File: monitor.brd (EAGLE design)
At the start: 149.3 x 84.8 mm, 60 parts, among them IC1 LM1117-5, IC2 LM1117-5, J3 DCJ0202, J4 DCJ0202, J5 DCJ0202, Q1 IRLML2502, T1 BC846, X3 PN61729-S, X4 PN87520-S

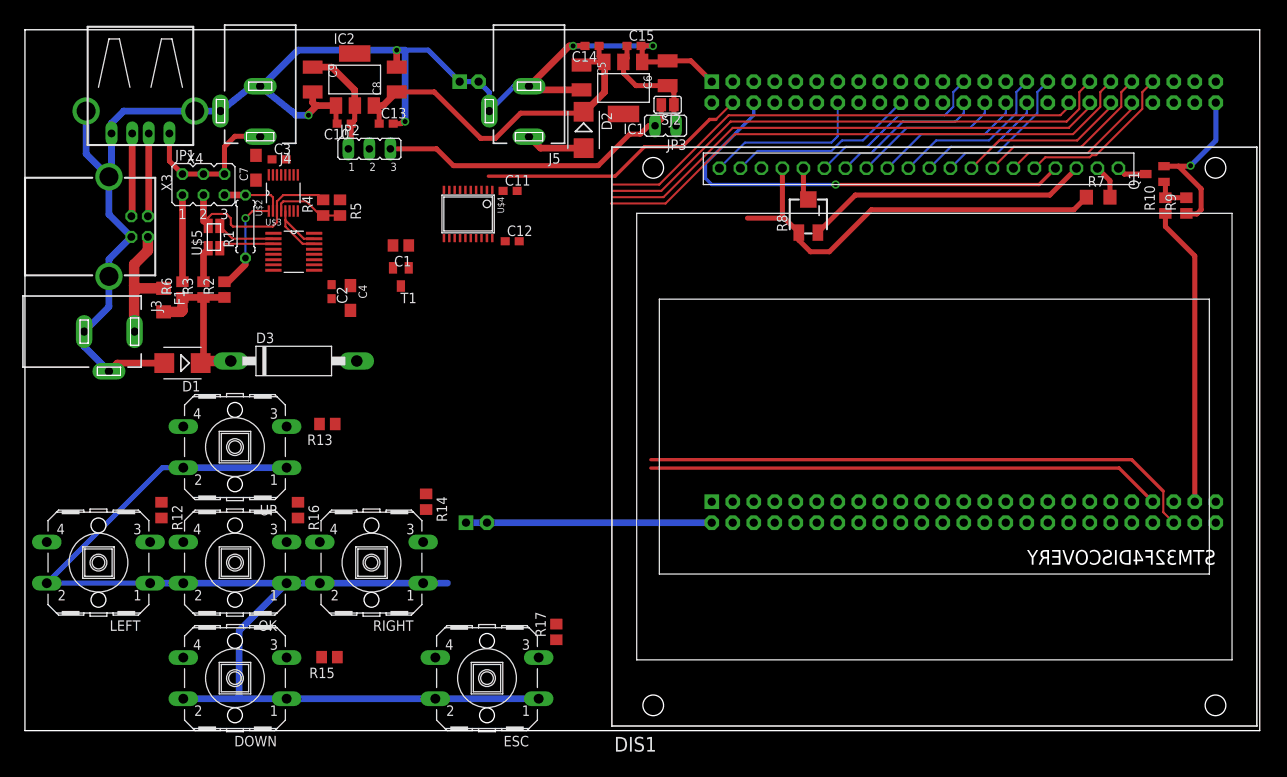
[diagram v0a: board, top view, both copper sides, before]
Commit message: SPI to PGA
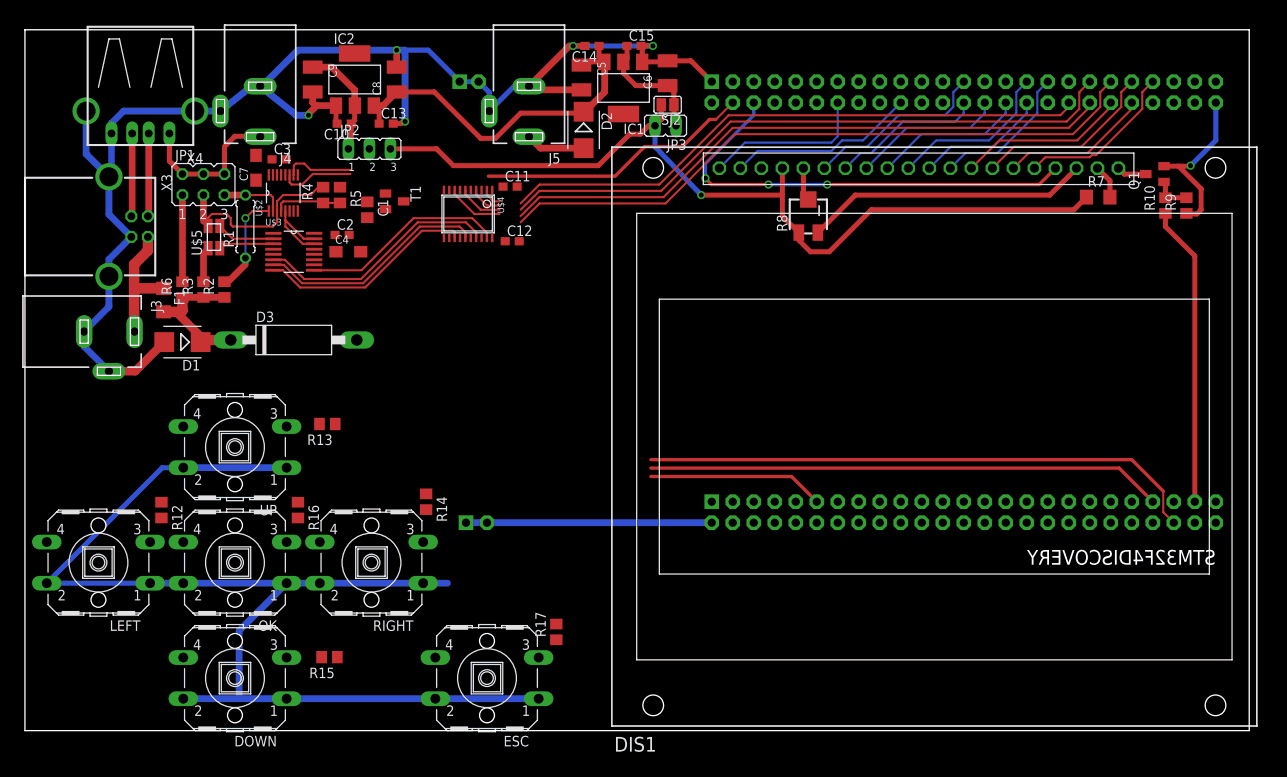
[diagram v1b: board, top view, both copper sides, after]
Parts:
- moved T1 9.18 mm to (44.7, 64.0), turned to 270 degrees
- moved C2 6.97 mm to (38.4, 59.9), turned to 0 degrees
- moved C1 5.93 mm to (41.4, 63.0), turned to 270 degrees
- moved C4 5.59 mm to (39.1, 57.9), turned to 0 degrees
- moved D1 2.54 mm to (19.1, 47.0)
- moved D3 2.54 mm to (32.5, 47.2)
- moved R4 1.52 mm to (36.1, 64.8)
- moved R5 1.52 mm to (38.1, 64.8)
- moved C11 0.51 mm to (58.7, 65.8)
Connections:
- new net OE: U$1.P$61, U$4.11
- net /CS: now also U$4.17; no longer U$4.19
- net CLK: now also U$4.13; no longer U$4.3
- net DIN: now also U$4.15; no longer U$4.5
- net DOUT: now also U$4.19; no longer U$4.17
- net I2C3_SCL: now also U$4.12; no longer U$4.14
- net I2C3_SDA: now also U$4.14; no longer U$4.6
- net SCL: now also U$4.9; no longer U$4.7
- net SDA: now also U$4.7; no longer U$4.15
- net SPI2_MISO: now also U$4.2; no longer U$4.4
- net SPI2_MOSI: now also U$4.6; no longer U$4.16
- net SPI2_NSS: now also U$4.4; no longer U$4.2
- net SPI2_SCK: now also U$4.8; no longer U$4.18
- net VDD: no longer U$1.P$72
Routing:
- net /CS: track 0.00 -> 29.5 mm
- net DIN: track 0.00 -> 28.0 mm
- net CLK: track 0.00 -> 26.4 mm
- net DOUT: track 0.00 -> 24.9 mm
- net OE: track 0.00 -> 21.3 mm
- net SPI2_SCK: track 64.3 -> 83.4 mm
- net SPI2_MOSI: track 67.6 -> 84.9 mm
- net +5V: track 90.2 -> 106.4 mm, vias 0 -> 1
- net SPI2_NSS: track 59.5 -> 75.6 mm
- net SPI2_MISO: track 62.7 -> 77.3 mm
- net SCL: track 0.00 -> 8.91 mm
- net SDA: track 0.00 -> 8.41 mm
- net N$13: track 20.8 -> 19.4 mm
- net GND: track 370.5 -> 371.6 mm
- net V_SENSE_HALF: track 8.84 -> 8.21 mm
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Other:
- board size 149.3 x 84.8 mm -> 148.1 x 84.8 mm

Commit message: All chips connected
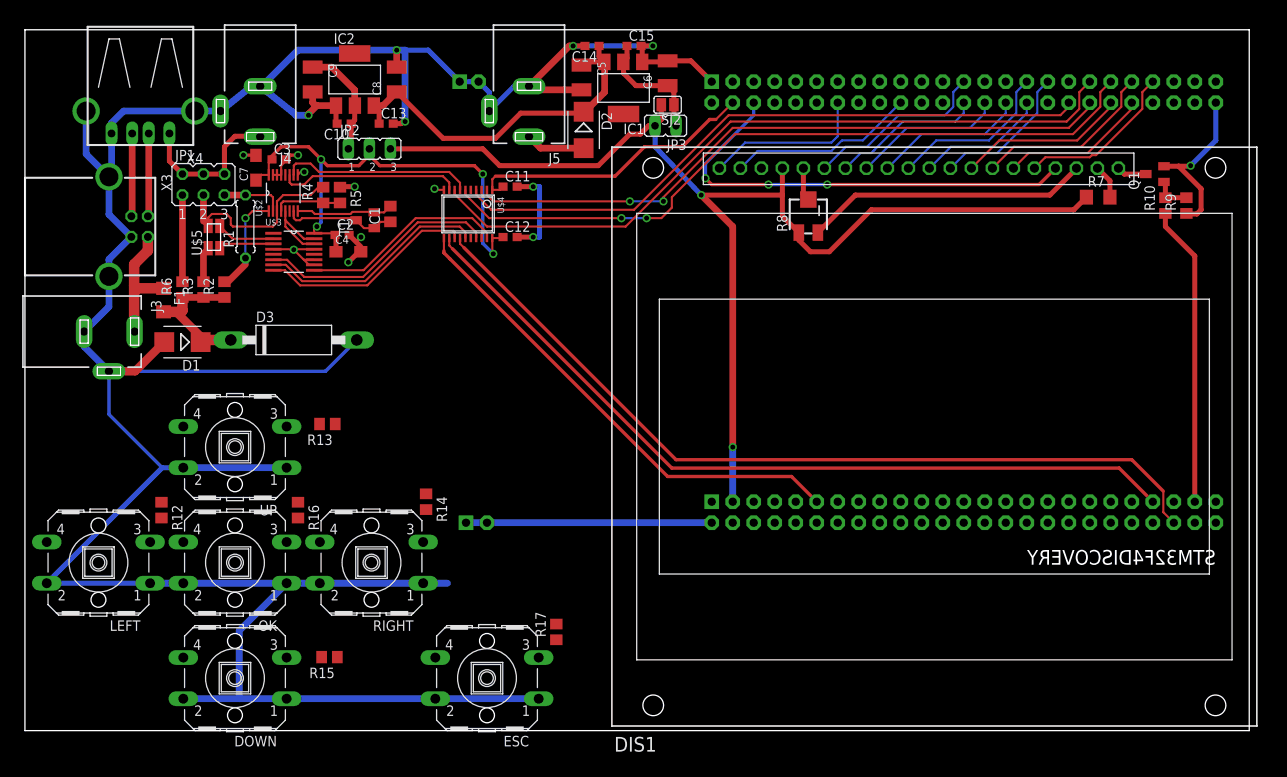
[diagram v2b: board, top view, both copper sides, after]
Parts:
- moved T1 4.23 mm to (41.1, 61.7), turned to 90 degrees
- moved C1 2.84 mm to (44.2, 62.5), turned to 90 degrees
- moved C12 0.57 mm to (58.7, 59.7)
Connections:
- net OUT: no longer U$2.6
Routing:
- net GND: track 371.6 -> 451.2 mm, vias 6 -> 14
- net VCC: track 0.00 -> 61.1 mm, vias 0 -> 4
- net +5V: track 106.4 -> 145.0 mm, vias 1 -> 2
- net OE: track 21.3 -> 59.9 mm
- net I2C3_SCL: track 62.4 -> 100.1 mm
- net I2C3_SDA: track 67.9 -> 102.5 mm
- net SDA: track 8.41 -> 23.2 mm
- net N$14: track 0.00 -> 13.6 mm
- net SCL: track 8.91 -> 22.0 mm
- net N$15: track 0.00 -> 11.8 mm
- net SPI2_SCK: track 83.4 -> 87.4 mm
- net SPI2_MOSI: track 84.9 -> 88.4 mm, vias 0 -> 2
- net SPI2_NSS: track 75.6 -> 78.7 mm
- net VDD: track 33.2 -> 35.7 mm
- net SPI2_MISO: track 77.3 -> 79.4 mm, vias 0 -> 2
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
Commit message: All connected (not routed), updated STM32F4Discovery layout
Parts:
- moved R12 74.7 mm to (90.9, 20.6)
- moved R15 69.5 mm to (105.4, 20.1), turned to 270 degrees
- moved R16 63.1 mm to (95.8, 20.3)
- moved R13 53.5 mm to (87.4, 20.3), turned to 270 degrees
- moved R14 52.4 mm to (100.3, 20.1)
- moved R17 46.2 mm to (109.7, 20.1), turned to 270 degrees
- moved RIGHT 1.05 mm to (42.9, 20.6)
- moved OK 1.05 mm to (26.4, 20.6)
- moved DOWN 1.05 mm to (26.4, 6.60)
- moved UP 1.05 mm to (26.4, 34.5)
- moved LEFT 1.05 mm to (9.91, 20.6)
- moved ESC 1.05 mm to (56.9, 6.60)
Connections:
- net B_DOWN: now also U$1.P$74
- net B_ESC: now also U$1.P$76
- net B_LEFT: now also U$1.P$64
- net B_OK: now also U$1.P$66
- net B_RIGHT: now also U$1.P$69
- net B_UP: now also U$1.P$63
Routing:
- net GND: track 451.2 -> 526.0 mm, vias 14 -> 18
- net N$28: track 0.00 -> 10.2 mm
- net N$27: track 0.00 -> 10.2 mm
- net N$26: track 0.00 -> 10.2 mm
- net N$29: track 0.00 -> 10.2 mm
- net N$23: track 2.05 -> 0.00 mm, vias 1 -> 0
- net N$16: track 0.72 -> 0.00 mm, vias 1 -> 0
- added copper zone on layer 16, net GND
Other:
- board text added: "AGH 2013"

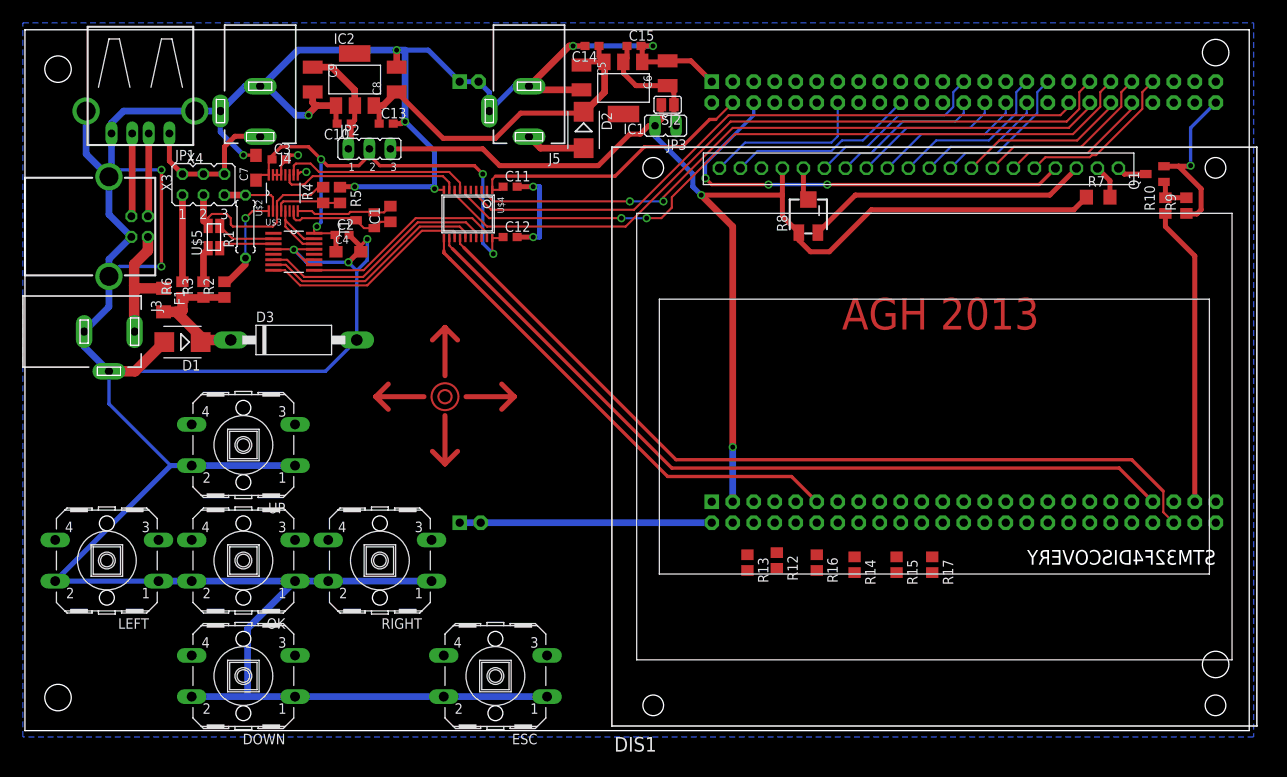
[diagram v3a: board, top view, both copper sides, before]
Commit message: All routed, drill diameter increased
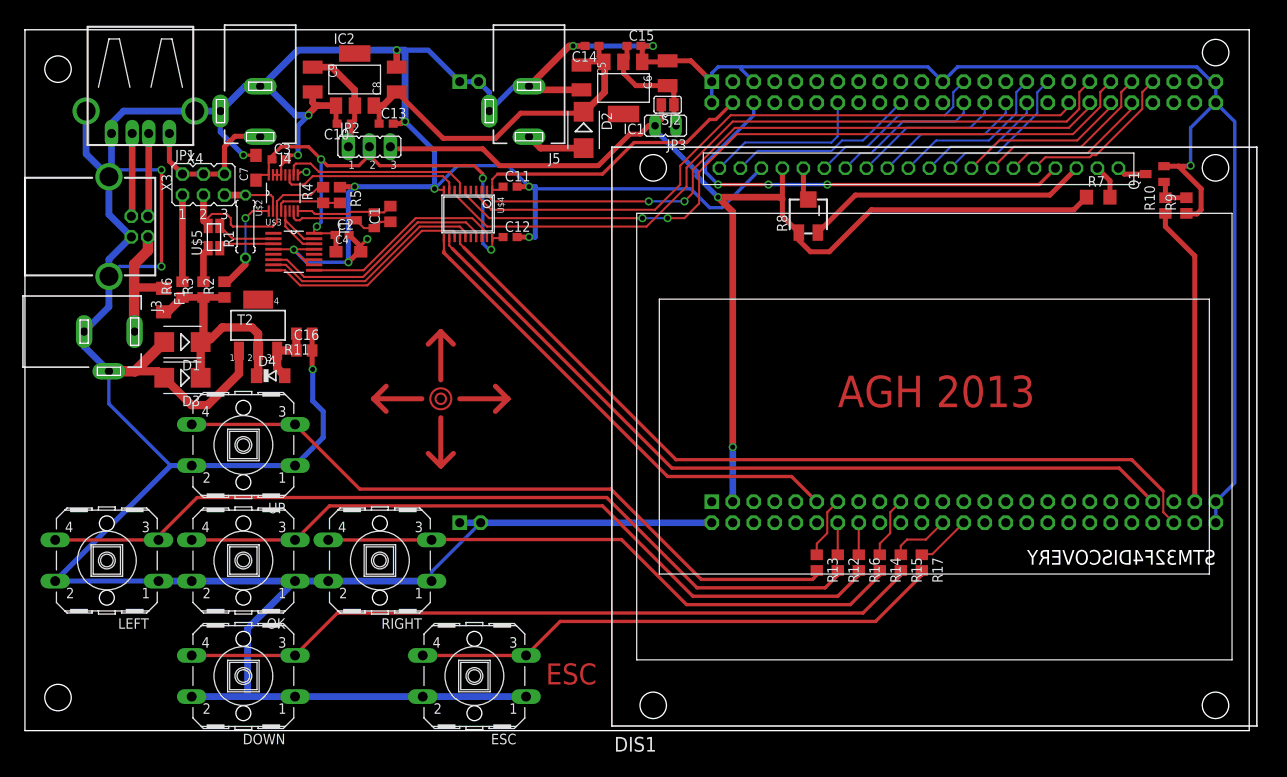
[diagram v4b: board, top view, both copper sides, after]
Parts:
- added C16: 1u, rcl:C0805
- added D4: 5V6, diode:SOD80C
- added R11: 4k7, rcl:R0805
- added T2: BT148, mgr_components:SOT223
- D3: value P6KE6.8CA -> SMBJ6.8CA; device diode:CB417-15 -> mgr_components:SMB
- F1: value 1.6A -> 1A
- moved D3 14.2 mm to (19.1, 42.7), turned to 180 degrees
- moved R13 8.38 mm to (95.8, 20.3)
- moved R12 7.37 mm to (98.3, 20.3)
- moved R16 5.08 mm to (100.8, 20.3)
- moved R14 3.06 mm to (103.4, 20.3)
- moved ESC 2.54 mm to (54.4, 6.60)
- moved R17 1.30 mm to (108.5, 20.3)
- moved R15 0.57 mm to (105.9, 20.3)
- moved JP2 0.25 mm to (41.7, 70.6)
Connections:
- new net N$23: C16.1, D4.A, R11.2, T2.3
- net GND: now also C16.2, R11.1, T2.1
- net N$13: now also D4.C, T2.2
- net N$17: now also UP.4
- net N$18: now also RIGHT.4
- net N$19: now also DOWN.4
- net N$20: now also ESC.4
- net N$21: now also OK.4
- net N$7: now also LEFT.4
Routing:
- net GND: track 526.0 -> 706.9 mm, vias 18 -> 19
- net N$7: track 0.00 -> 102.8 mm
- net N$19: track 0.00 -> 90.3 mm
- net N$21: track 0.00 -> 88.5 mm
- net N$17: track 0.00 -> 84.1 mm
- net N$18: track 0.00 -> 72.0 mm
- net N$20: track 0.00 -> 64.9 mm
- net N$13: track 19.4 -> 31.0 mm
- net N$16: track 0.00 -> 10.2 mm
- net N$27: track 10.2 -> 0.00 mm
- net N$23: track 0.00 -> 7.75 mm
- net B_UP: track 0.00 -> 7.47 mm
- net B_RIGHT: track 0.00 -> 7.47 mm
- net B_DOWN: track 0.00 -> 7.32 mm
- net B_ESC: track 0.00 -> 6.69 mm
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- removed copper zone on layer 16, net GND
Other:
- board text added: "ESC"

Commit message: Added inductors on analog supply. Rerouted some signals.
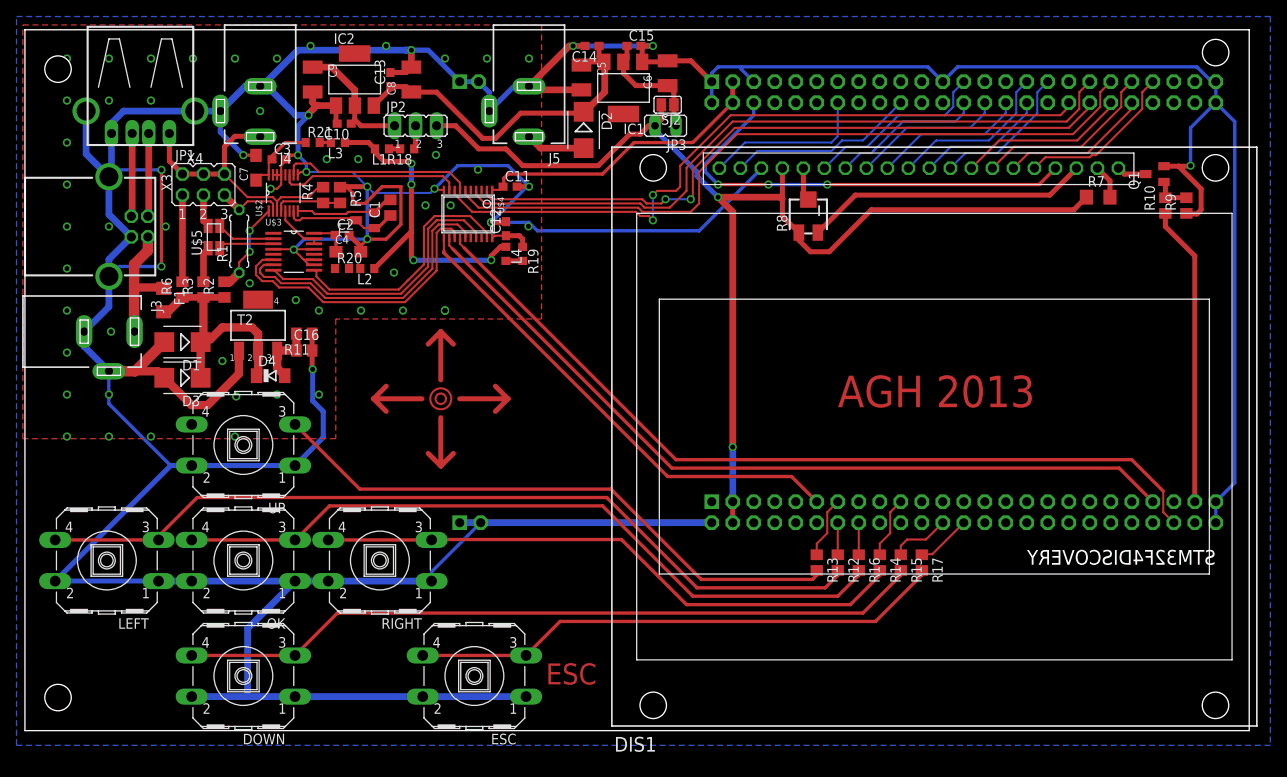
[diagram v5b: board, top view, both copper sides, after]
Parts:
- added L1, L2, L3, L4: 100n, rcl:R0603
- added R18, R19, R20, R21: 1R, rcl:R0603
- moved JP2 6.14 mm to (47.2, 73.2)
- moved C13 5.36 mm to (44.2, 78.7), turned to 90 degrees
- moved R1 1.93 mm to (25.9, 59.2)
- moved C8 1.78 mm to (46.7, 78.7)
- moved C12 1.14 mm to (58.2, 60.7), turned to 90 degrees
- moved C1 0.76 mm to (44.2, 63.2)
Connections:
- new net N$24: L1.1, R18.2
- new net N$25: JP2.2, R18.1
- new net N$27: C12.1, R19.1, U$4.20
- new net N$30: L4.2, R19.2
- new net N$31: C2.1, C4.+, R20.1, U$3.16
- new net N$32: C3.1, C7.+, R21.1, U$2.16
- new net N$33: L2.2, R20.2
- new net N$35: L3.2, R21.2
- net /CS: now also U$4.13; no longer U$4.17
- net CLK: now also U$4.17; no longer U$4.13
- net N$17: no longer UP.4
- net OUT: now also R4.2, U$2.3
- net SPI2_NSS: now also U$4.8; no longer U$4.4
- net SPI2_SCK: now also U$4.4; no longer U$4.8
- net VCC: now also L1.2, L2.1, L3.1, L4.1; no longer C12.1, C2.1, C3.1, C4.+, C7.+, JP2.2, U$2.16, U$3.16, U$4.20
- net V_SENSE: no longer R4.2, U$2.3
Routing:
- net VCC: track 60.4 -> 39.6 mm
- net V_SENSE: track 23.6 -> 3.97 mm
- net GND: track 706.9 -> 723.3 mm, vias 19 -> 68
- net OUT: track 18.8 -> 34.0 mm
- net N$17: track 84.1 -> 71.6 mm
- net N$32: track 0.00 -> 9.24 mm
- net DIN: track 27.8 -> 35.8 mm
- net CLK: track 26.2 -> 33.3 mm
- net /CS: track 29.3 -> 36.1 mm
- net SPI2_NSS: track 80.0 -> 85.6 mm, vias 0 -> 2
- net DOUT: track 24.9 -> 30.1 mm
- net N$27: track 0.00 -> 4.91 mm
- net N$31: track 0.00 -> 4.69 mm
- net PGA_OUT: track 10.6 -> 6.13 mm
- net SPI2_SCK: track 88.7 -> 84.6 mm
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- added copper zone on layer 1, net GND
- added copper zone on layer 16, net GND

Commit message: Extra vias
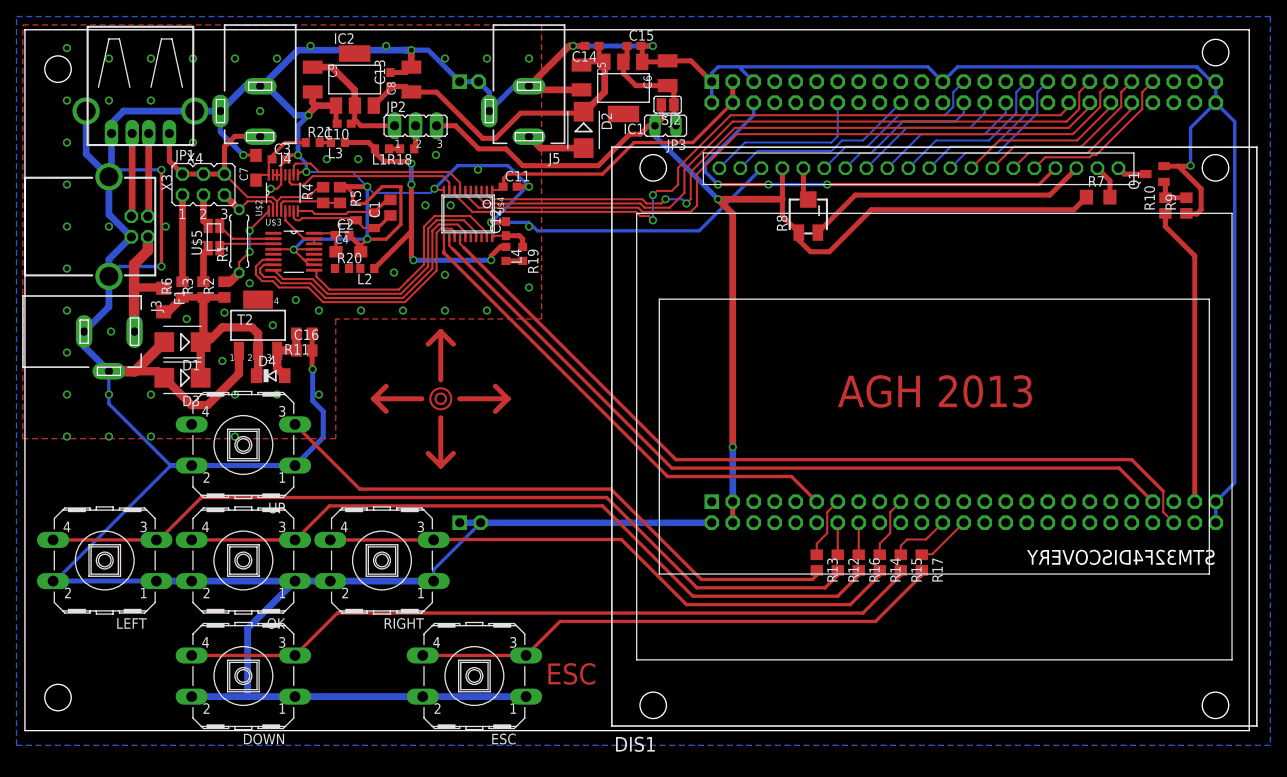
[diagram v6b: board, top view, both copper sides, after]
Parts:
- F1: value 1A -> 500m
- moved LEFT 0.25 mm to (9.65, 20.6)
- moved RIGHT 0.25 mm to (43.2, 20.6)
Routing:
- net GND: track 723.3 -> 724.0 mm, vias 68 -> 74

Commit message: minor improvements
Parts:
- moved LEFT 5.33 mm to (15.0, 20.6)
- moved DOWN 2.54 mm to (29.0, 6.60)
- moved ESC 2.54 mm to (56.9, 6.60)
- moved OK 2.54 mm to (29.0, 20.6), turned to 90 degrees
- moved UP 2.54 mm to (29.0, 34.5)
- moved C10 0.80 mm to (37.8, 73.2)
- moved L1 0.76 mm to (43.2, 71.1)
- moved R18 0.76 mm to (46.2, 71.1)
- moved JP2 0.51 mm to (47.2, 73.7)
- moved R5 0.36 mm to (37.8, 64.5)
- moved R4 0.36 mm to (35.8, 64.5)
- moved RIGHT 0.25 mm to (42.9, 20.6)
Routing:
- net GND: track 724.0 -> 611.8 mm, vias 74 -> 76
- net N$19: track 90.3 -> 87.8 mm
- net N$20: track 64.9 -> 62.4 mm
- net N$31: track 4.69 -> 6.77 mm
- net N$17: track 71.6 -> 69.8 mm
- net N$33: track 0.00 -> 1.35 mm
- net VCC: track 39.6 -> 40.8 mm
- net N$10: track 15.6 -> 16.4 mm
